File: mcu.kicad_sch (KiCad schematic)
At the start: 35 parts, among them J2 Conn_02x07_Odd_Even, J4 USB_C_Receptacle_USB2.0_16P, J7 Conn_02x06_Counter_Clockwise, SW3 SW_Push, U1 BME280, U6 USBLC6-2SC6, U7 STM32U535CBTxQ, Y1 32.768KHz, Y2 16MHz

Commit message: footprint assignment
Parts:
- C12, C14, C15, C16, C18, C6: footprint Capacitor_SMD:C_0402_1005Metric_Pad0.74x0.62mm_HandSolder -> Capacitor_SMD:C_0603_1608Metric_Pad1.08x0.95mm_HandSolder
- L1: footprint Inductor_SMD:L_0402_1005Metric_Pad0.77x0.64mm_HandSolder -> Inductor_SMD:L_0805_2012Metric_Pad1.05x1.20mm_HandSolder
- Y1: footprint Crystal:Crystal_SMD_0603-2Pin_6.0x3.5mm_HandSoldering -> Crystal:Crystal_SMD_MicroCrystal_CM9V-T1A-2Pin_1.6x1.0mm_HandSoldering
- Y2: footprint Crystal:Crystal_SMD_0603-2Pin_6.0x3.5mm_HandSoldering -> Crystal:Crystal_SMD_2016-4Pin_2.0x1.6mm
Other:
- moved on the sheet: C44, C50, C51, J7, R10, R9, SW3, U1

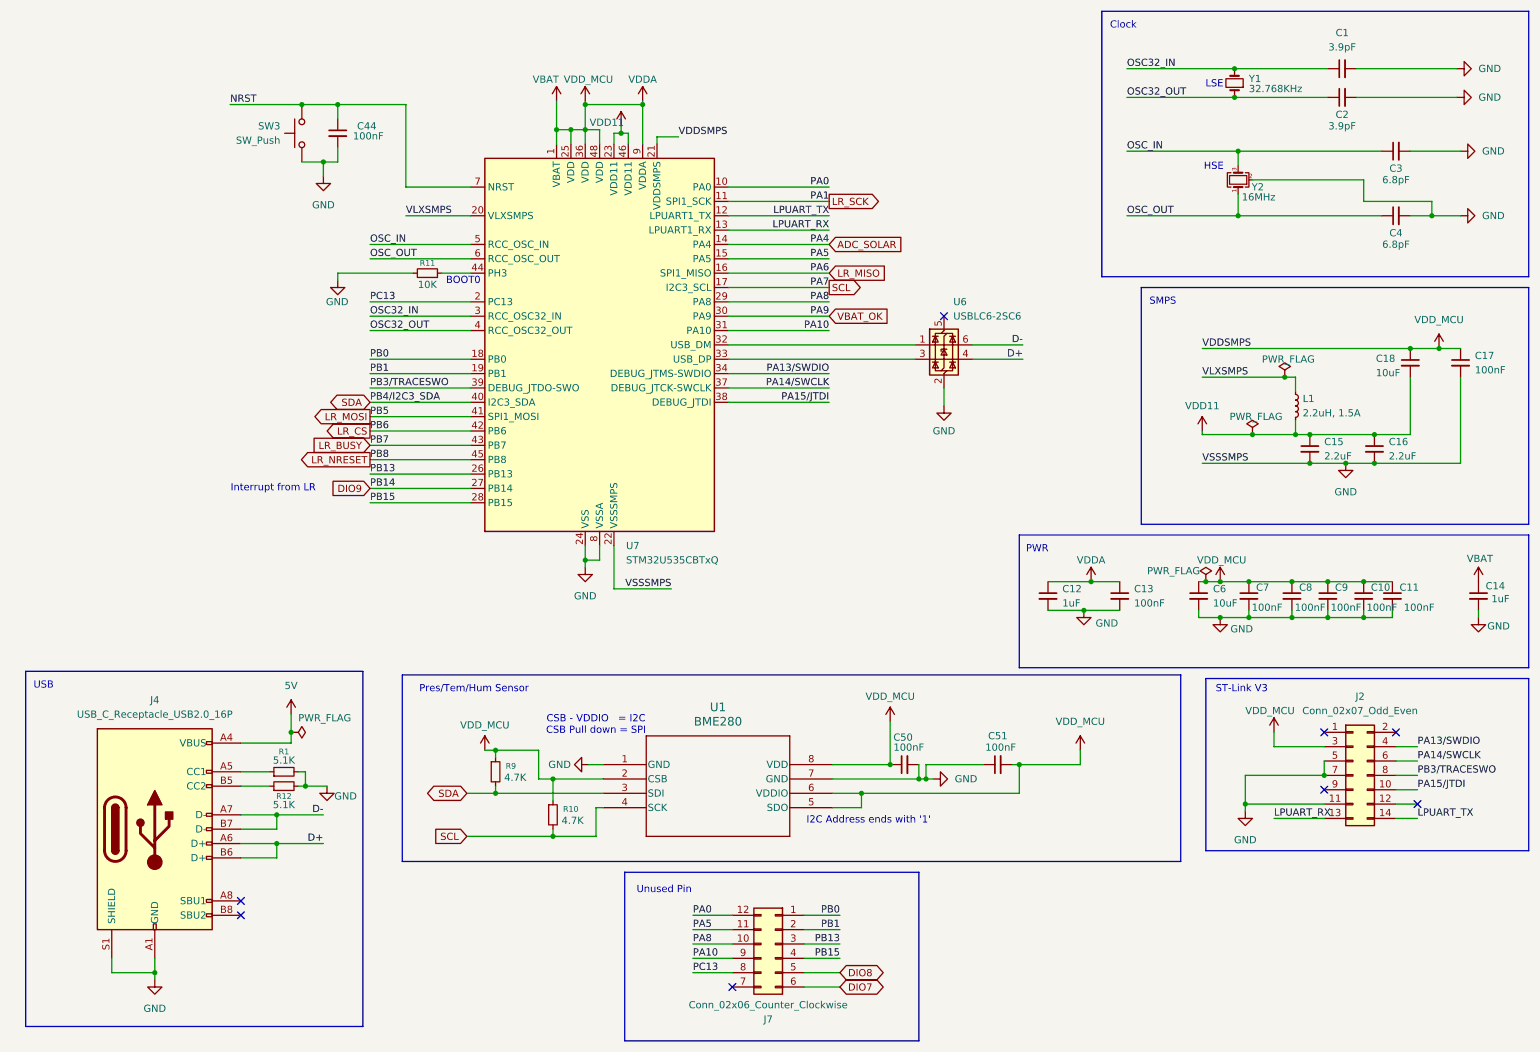
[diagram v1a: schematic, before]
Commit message: RF and initial routing
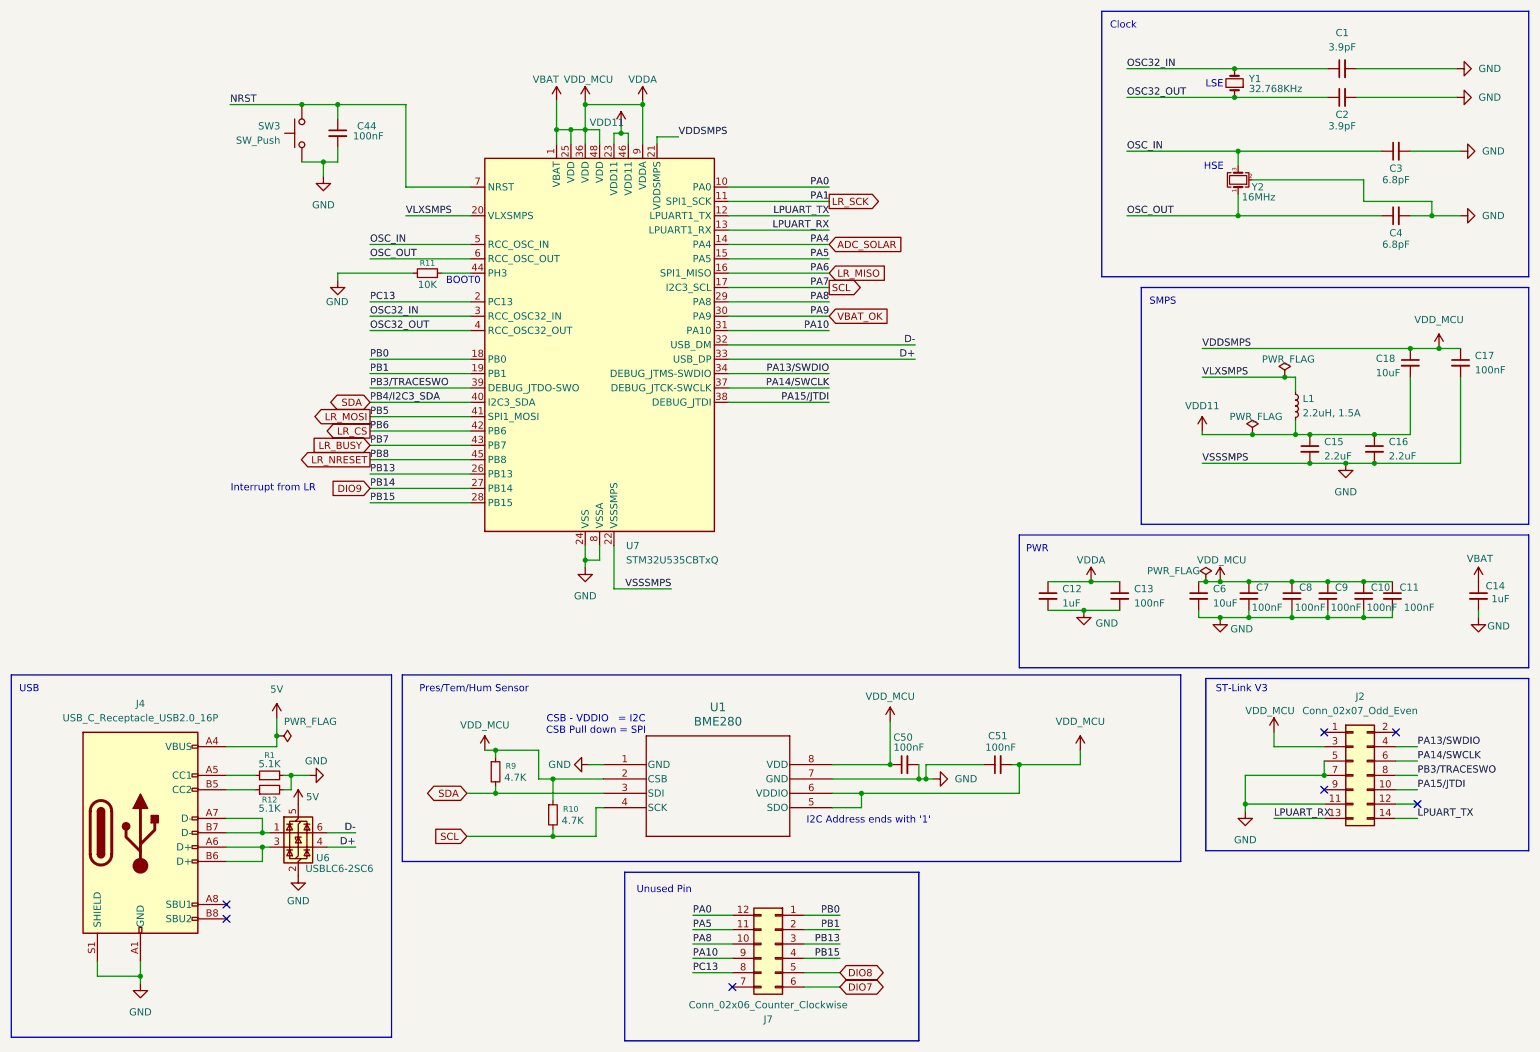
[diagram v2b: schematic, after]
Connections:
- net 5V: now also U6.5 (VBUS)
- net D+: now also U7.33 (PA12); no longer J4.A6 (D+), J4.B6 (D+)
- net D-: now also U7.32 (PA11); no longer J4.A7 (D-), J4.B7 (D-)
- net at U6.1 (I/O1): now also J4.A7 (D-), J4.B7 (D-); no longer U7.32 (PA11)
- net at U6.3 (I/O2): now also J4.A6 (D+), J4.B6 (D+); no longer U7.33 (PA12)
- no-connect marks 8 -> 7
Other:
- moved on the sheet: J4, R1, R12, U6

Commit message: changed RF switch in schematics, todo in pcb
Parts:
- J2: footprint Connector_PinHeader_1.27mm:PinHeader_2x07_P1.27mm_Vertical -> Connector_PinHeader_1.27mm:PinHeader_2x07_P1.27mm_Vertical_SMD
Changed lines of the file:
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@@
 			)
 		)
-		(property "Footprint" "Connector_PinHeader_1.27mm:PinHeader_2x07_P1.27mm_Vertical"
+		(property "Footprint" "Connector_PinHeader_1.27mm:PinHeader_2x07_P1.27mm_Vertical_SMD"
 			(at 251.46 149.86 0)
 			(effects

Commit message: fix smtp line and minor errors
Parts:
- L1: value 2.2uH, 1.5A -> 2.2uH
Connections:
- net GND: now also C18.2
- net VDD11: no longer C18.2
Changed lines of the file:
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@@
 	)
 	(junction
-		(at 255.27 89.535)
-		(diameter 0)
-		(color 0 0 0 0)
-	)
-	(junction
 		(at 125.73 31.115)
 		(diameter 0)
@@
 	)
 	(junction
+		(at 261.62 94.615)
+		(diameter 0)
+		(color 0 0 0 0)
+	)
+	(junction
 		(at 232.41 154.94)
 		(diameter 0)
@@
 	(wire
 		(pts
-			(xy 261.62 79.375) (xy 261.62 89.535)
+			(xy 261.62 79.375) (xy 261.62 94.615)
 		)
 		(stroke
@@
 	(wire
 		(pts
-			(xy 261.62 89.535) (xy 255.27 89.535)
-		)
-		(stroke
-			(width 0)
-			(type default)
-		)
-	)
-	(wire
-		(pts
 			(xy 253.365 115.57) (xy 258.445 115.57)
 		)
@@
 	(wire
 		(pts
-			(xy 270.51 94.615) (xy 255.27 94.615)
+			(xy 270.51 94.615) (xy 261.62 94.615)
 		)
 		(stroke
@@
 	(wire
 		(pts
+			(xy 261.62 94.615) (xy 255.27 94.615)
+		)
+		(stroke
+			(width 0)
+			(type default)
+		)
+	)
+	(wire
+		(pts
 			(xy 77.47 99.06) (xy 95.25 99.06)
 		)
@@
 			)
 		)
-		(property "Value" "2.2uH, 1.5A"
+		(property "Value" "2.2uH"
 			(at 242.57 85.7249 0)
 			(effects

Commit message: V0.1
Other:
- note added: "Further improvement: use SPI also for BME and switch to the low power one."
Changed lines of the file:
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@@
+		)
+	)
+	(text "Further improvement:\nuse SPI also for BME and \nswitch to the low power one."
+		(exclude_from_sim no)
+		(at 191.77 160.02 0)
+		(effects
+			(font
+				(size 1.27 1.27)
+			)
+			(justify left)
 		)
 	)
